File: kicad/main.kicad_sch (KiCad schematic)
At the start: 37 parts, among them J1 Barrel_Jack, SW1 Reset, SW2 SW_DIP_x08, U1 KM1810VM88, U10 L7805, U11 15 MHz, U12 8255, U2 W27C512, U3 AS6C4008-55PCN, U4 74HC573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

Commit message: Corrected version of v1 PCB
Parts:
- added J2: ~, Connector_PinHeader_2.54mm:PinHeader_1x04_P2.54mm_Vertical, symbol Connector:Conn_01x04_Pin
- added R1: 10K, Resistor_THT:R_Axial_DIN0207_L6.3mm_D2.5mm_P10.16mm_Horizontal, symbol Device:R
- added R4, R5: 10K, Resistor_THT:R_Axial_DIN0204_L3.6mm_D1.6mm_P7.62mm_Horizontal, symbol Device:R
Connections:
- net +5V: now also J2.2 (Pin_2), R4.1, R5.1
- net GND: now also J2.1 (Pin_1), R1.2
- net at RN1.4 (R3.2): no longer U1.18 (INTR)
- net at U12.11 (PC6): now also LCD1.6 (E)
- net at U12.12 (PC5): now also LCD1.5 (R~{W})
- net at U12.13 (PC4): now also LCD1.4 (RS)
- net INT: now reaches U12.14 (PC0)
- net INT: now also U1.18 (INTR), R1.1
- net PS2CLK: now reaches U12.16 (PC2)
- net PS2CLK: now also J2.3 (Pin_3), R4.2
- net PS2DATA: now reaches U12.18 (PB0)
- net PS2DATA: now also J2.4 (Pin_4), R5.2; no longer LCD1.4 (RS)
- net at U12.19 (PB1): no longer LCD1.5 (R~{W})
- net at U12.20 (PB2): no longer LCD1.6 (E)
- no-connect marks 36 -> 34
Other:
- note added: "0"
- note added: "0 if mode set flag"
- note added: "0,1"
- note added: "1"
- note added: "1 if bit set flag"
- note added: "8255 interrupt config: http://jap.hu/electronic/8255.pdf Page 11"
- note added: "Address decoder & clock"
- note added: "Group A"
- note added: "Group B"
- note added: "IBF_{B}"
- note added: "INTR_{B}"
- note added: "Mode = 0"
- note added: "Mode = 1 (strobe)"
- note added: "PC_{2} <- 1 (enable interrupts on Group B)"
- note added: "PS/2 keyboard"
- note added: "Port A = IN & OUT"
- note added: "Port B = INPUT"
- note added: "Port C (high) = OUTPUT"
- note added: "Port C (low) = N/C"
- note added: "X"
- note added: "~{STB}_{B}"
- note removed: "Address decoder & clock generator"
- moved on the sheet: BAR1, C2, C3, C4, C5, C6, D1, D2, LCD1, R2, R3, RN1A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

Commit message: Mark as v02
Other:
- title: (none) -> ПК-88
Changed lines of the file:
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@@
 (kicad_sch (version 20230121) (generator eeschema)
   (paper "A3")
+  (title_block
+    (title "ПК-88")
+    (date "2023-09-28")
+    (rev "v0.2")
+  )
   (junction (at 322.58 223.52) (diameter 0) (color 0 0 0 0)
   )

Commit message: Add I/O sheet
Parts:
- removed BAR1: HDSP-4830_2, Display:HDSP-4830, symbol LED:HDSP-4830_2
- removed J2: ~, Connector_PinHeader_2.54mm:PinHeader_1x04_P2.54mm_Vertical, symbol Connector:Conn_01x04_Pin
- removed LCD1: ~, footprints:2004A-OLED, symbol lcd:2004A-OLED
- removed R1: 10K, Resistor_THT:R_Axial_DIN0207_L6.3mm_D2.5mm_P10.16mm_Horizontal, symbol Device:R
- removed R4, R5: 10K, Resistor_THT:R_Axial_DIN0204_L3.6mm_D1.6mm_P7.62mm_Horizontal, symbol Device:R
- removed RN2: 330R, Resistor_THT:R_Array_SIP9, symbol Device:R_Network08
- removed RN3: 5K, Resistor_THT:R_Array_SIP9, symbol Device:R_Network08
- removed SW2: SW_DIP_x08, Button_Switch_THT:SW_DIP_SPSTx08_Slide_9.78x22.5mm_W7.62mm_P2.54mm, symbol Switch:SW_DIP_x08
- removed U12: 8255, Package_DIP:DIP-40_W15.24mm_Socket, symbol Interface:8255
- removed U6: ATF16V8, Package_DIP:DIP-20_W7.62mm_Socket, symbol Logic_Programmable:GAL16V8
- removed U6: 74HC273, Package_DIP:DIP-20_W7.62mm_Socket, symbol 74xx:74HC273
- removed U8: 74HC00, Package_DIP:DIP-14_W7.62mm_Socket, symbol 74hc00_small:74HC00
- added U6: GAL22V10, Package_DIP:DIP-24_W7.62mm_Socket, symbol my:GAL22V10
- added U8: 74HC14, Package_DIP:DIP-14_W7.62mm_Socket, symbol 74hc00_small:74HC14_small
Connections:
- net +5V: now also U6.24 (VCC), U8.14 (VCC)
- net A_{16}: now also U6.3 (I)
- net A_{17}: now also U6.4 (I)
- net A_{18}: now also U6.5 (I)
- net A_{19}: now also U6.6 (I)
- net A_{8}: now also U6.2 (I)
- net CLK: now also U8.2
- net GND: now also U6.12 (GND), U6.13 (I), U8.13, U8.7 (GND)
- net IN~{EN}: now also U6.20 (I/O/Q)
- net IO/~{M}: now also U6.9 (I)
- net IO~{EN}: now also U6.19 (I/O/Q)
- net OUT~{EN}: now also U6.21 (I/O/Q)
- net RAM~{EN}: now also U6.22 (I/O/Q)
- net RES: now also U8.6
- net ROM~{EN}: now also U6.23 (I/O/Q)
- net ~{RD}: now also U6.7 (I)
- net ~{WR}: now also U6.8 (I)
- net at U11.10, U11.8 (OUT), U11.9: now also U6.1 (I/CLK)
- net ~{INTA}: now reaches U1.24 (~{INTA})
- net ~{RES}: now reaches SW1.1, U7.1 (~{RST})
- net ~{RES}: now also U8.5
- net INT renamed INTR
- new net: U6.17 (I/O/Q), U8.3
- new net: U6.15 (I/O/Q), U8.1
- new net TIMERCLK: U8.4
- new net TIMER~{EN}: U6.18 (I/O/Q)
- no-connect marks 34 -> 19
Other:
- added sheet IO & Interrupts (io.kicad_sch)
- note removed: "0"
- note removed: "0 if mode set flag"
- note removed: "0,1"
- note removed: "1"
- note removed: "1 if bit set flag"
- note removed: "8255 interrupt config: http://jap.hu/electronic/8255.pdf Page 11"
- note removed: "Group A"
- note removed: "Group B"
- note removed: "I/O controller"
- note removed: "I/O register"
- note removed: "IBF_{B}"
- note removed: "INTR_{B}"
- note removed: "Mode = 0"
- note removed: "Mode = 1 (strobe)"
- note removed: "PC_{2} <- 1 (enable interrupts on Group B)"
- note removed: "PS/2 keyboard"
- note removed: "Port A = IN & OUT"
- note removed: "Port B = INPUT"
- note removed: "Port C (high) = OUTPUT"
- note removed: "Port C (low) = N/C"
- note removed: "X"
- note removed: "~{STB}_{B}"
- moved on the sheet: D1, D2, R2, R3, U11, U2, U3, U4, U5

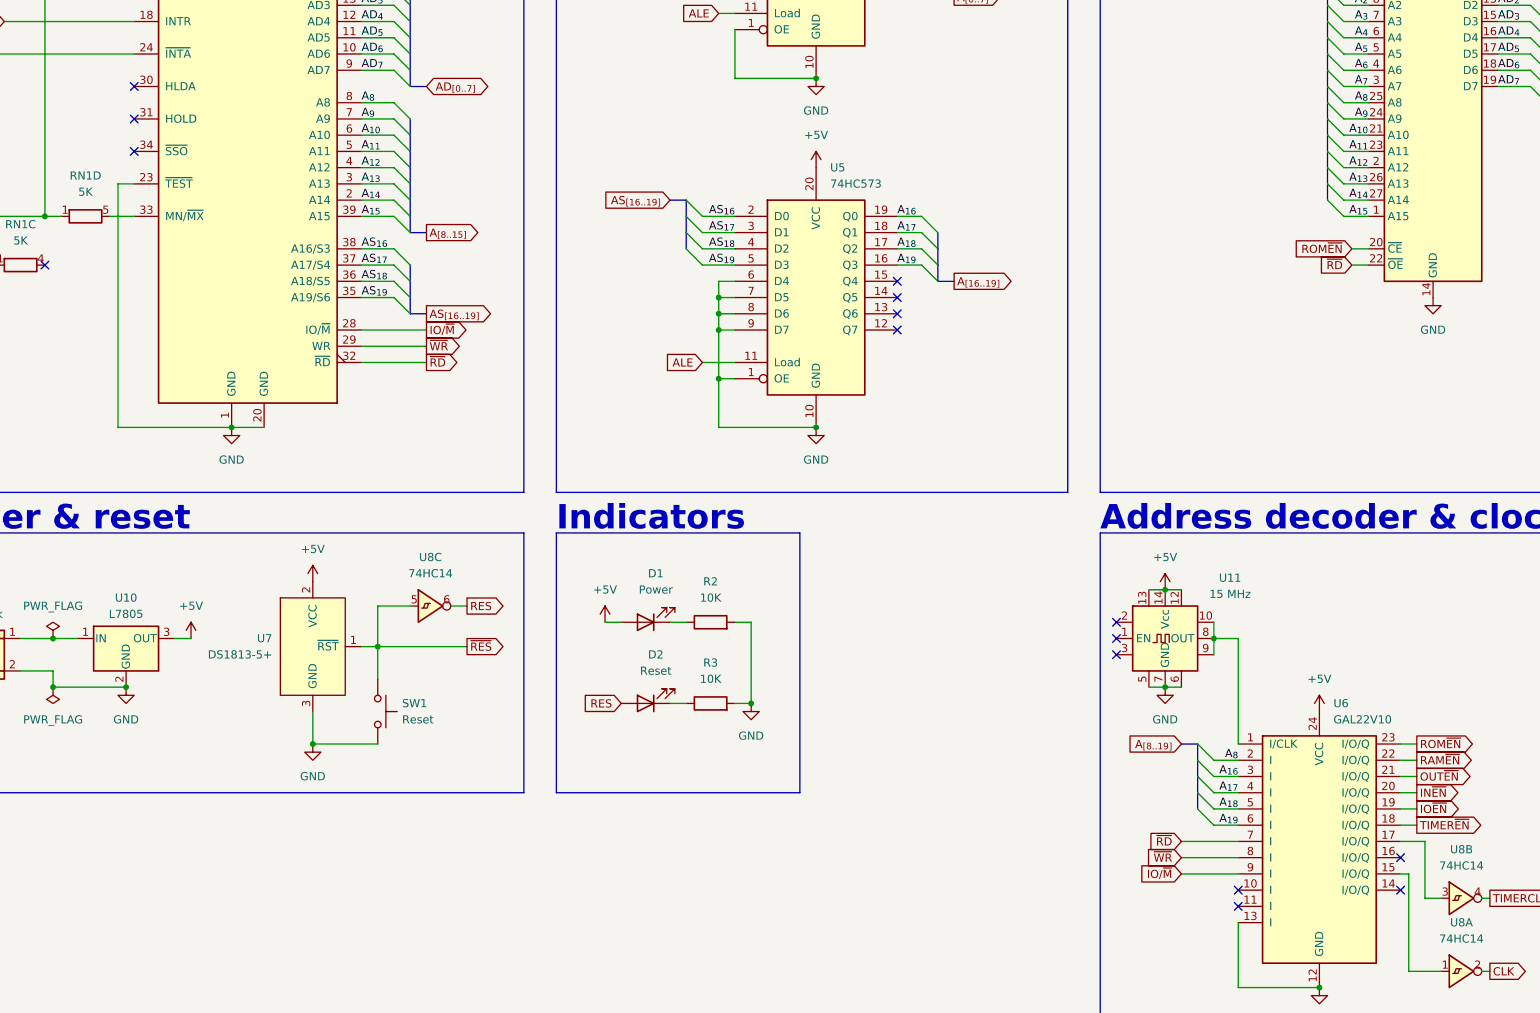
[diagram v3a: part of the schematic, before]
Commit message: Tie HOLD low, add GAL simulation for clock, add 8253 clock
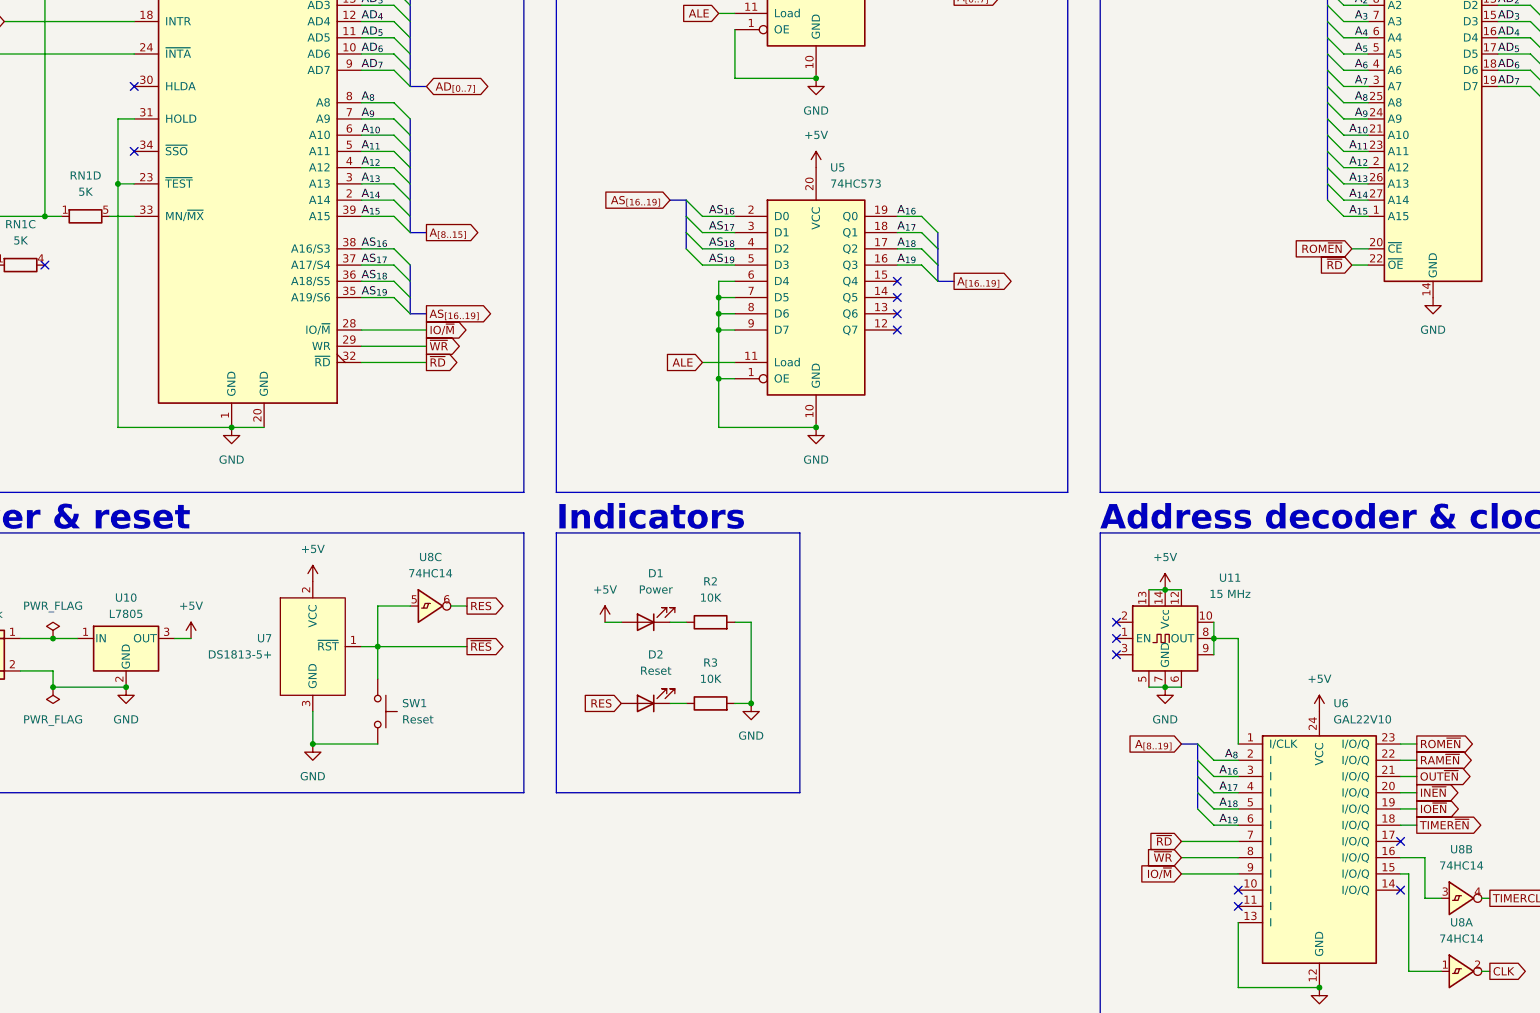
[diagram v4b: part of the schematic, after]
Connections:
- net GND: now also U1.31 (HOLD)
- net at U8.3: now also U6.16 (I/O/Q); no longer U6.17 (I/O/Q)
- no-connect marks 19 -> 18
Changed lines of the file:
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@@
   (junction (at 347.98 242.57) (diameter 0) (color 0 0 0 0)
+  )
+  (junction (at 48.26 86.36) (diameter 0) (color 0 0 0 0)
   )
   (junction (at 335.28 215.9) (diameter 0) (color 0 0 0 0)
@@
   (no_connect (at 25.4 167.64))
   (no_connect (at 36.83 99.06))
-  (no_connect (at 248.92 191.77))
+  (no_connect (at 248.92 189.23))
   (no_connect (at 50.8 71.12))
   (no_connect (at 223.52 199.39))
@@
   (no_connect (at 248.92 196.85))
   (no_connect (at 50.8 81.28))
-  (no_connect (at 50.8 76.2))
   (no_connect (at 86.36 43.18))
   (no_connect (at 170.18 106.68))
@@
     (stroke (width 0) (type default))
   )
-  (wire (pts (xy 252.73 189.23) (xy 252.73 198.12))
-    (stroke (width 0) (type default))
-  )
   (bus (pts (xy 137.16 93.98) (xy 137.16 91.44))
     (stroke (width 0) (type default))
@@
     (stroke (width 0) (type default))
   )
+  (wire (pts (xy 252.73 191.77) (xy 252.73 198.12))
+    (stroke (width 0) (type default))
+  )
   (wire (pts (xy 383.54 220.98) (xy 386.08 220.98))
     (stroke (width 0) (type default))
@@
     (stroke (width 0) (type default))
   )
-  (wire (pts (xy 248.92 189.23) (xy 252.73 189.23))
+  (wire (pts (xy 248.92 191.77) (xy 252.73 191.77))
     (stroke (width 0) (type default))
   )
@@
     (stroke (width 0) (type default))
   )
+  (wire (pts (xy 50.8 76.2) (xy 48.26 76.2))
+    (stroke (width 0) (type default))
+  )
   (bus (pts (xy 137.16 96.52) (xy 137.16 93.98))
     (stroke (width 0) (type default))
@@
     (stroke (width 0) (type default))
   )
+  (wire (pts (xy 48.26 76.2) (xy 48.26 86.36))
+    (stroke (width 0) (type default))
+  )

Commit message: Add UART
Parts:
- removed unit 6 of U8
- added U18: 1.8432 MHz, footprints:Oscillator_DIP-8-14, symbol my:CXO_DIP-8-14
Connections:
- net IN~{EN} is gone; now on net TIMER~{EN}: U6.20 (I/O/Q)
- net OUT~{EN} is gone; now on net IO~{EN}: U6.21 (I/O/Q)
- net +5V: now also U18.12, U18.13, U18.14 (Vcc)
- net A_{16}: now also U6.4 (I); no longer U6.3 (I)
- net A_{17}: now also U6.5 (I); no longer U6.4 (I)
- net A_{18}: now also U6.6 (I); no longer U6.5 (I)
- net A_{19}: now also U6.7 (I); no longer U6.6 (I)
- net A_{9}: now also U6.3 (I)
- net GND: now also U18.5, U18.6, U18.7 (GND)
- net IO/~{M}: now also U6.10 (I); no longer U6.9 (I)
- net IO~{EN}: no longer U6.19 (I/O/Q)
- net TIMER~{EN}: no longer U6.18 (I/O/Q)
- net ~{RD}: now also U6.8 (I); no longer U6.7 (I)
- net ~{WR}: now also U6.9 (I); no longer U6.8 (I)
- net MCLK: now reaches U11.10, U11.8 (OUT), U11.9, U6.1 (I/CLK)
- new net UARTCLK: U18.10, U18.8 (OUT), U18.9
- new net UART~{EN}: U6.19 (I/O/Q)
- no-connect marks 18 -> 20
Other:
- moved on the sheet: U8A, U8B

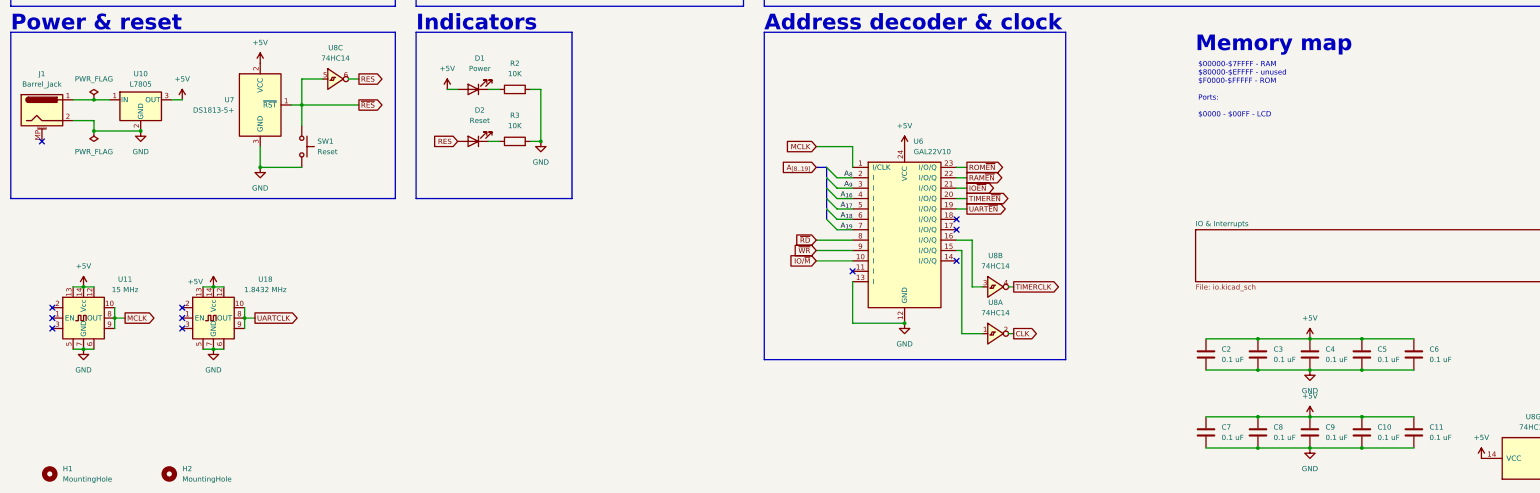
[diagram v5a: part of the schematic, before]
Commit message: Add UART & uSD card
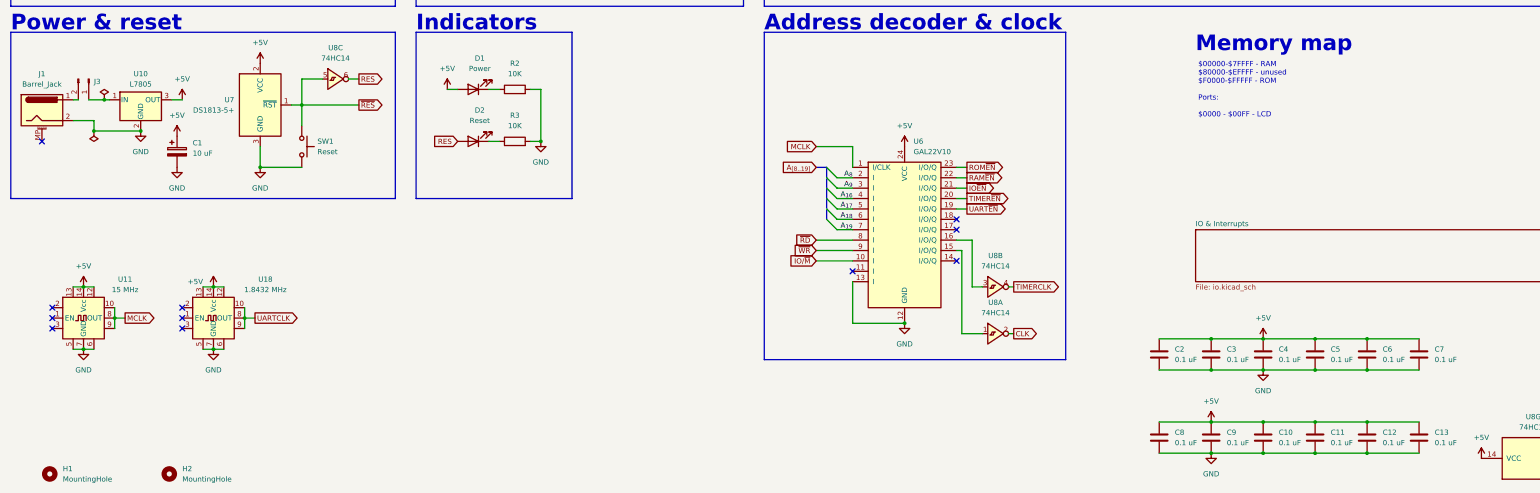
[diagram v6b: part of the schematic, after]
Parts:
- added C1: 10 uF, Capacitor_THT:CP_Radial_D8.0mm_P3.50mm, symbol Device:C_Polarized
- added C12, C13: 0.1 uF, footprints:C_Disc_Long, symbol Device:C
- added J3: ~, Connector_PinHeader_2.54mm:PinHeader_1x02_P2.54mm_Vertical, symbol Connector:Conn_01x02_Pin
- C9: footprint footprints:C_Disc_Long -> footprints:C_Disc_VeryLong
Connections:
- net +5V: now also C1.1, C12.1, C13.1
- net GND: now also C1.2, C12.2, C13.2
- net at U10.1 (IN): now also J3.1 (Pin_1); no longer J1.1
- new net: J1.1, J3.2 (Pin_2)
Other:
- moved on the sheet: C10, C11, C2, C3, C4, C5, C6, C7, C8, C9
